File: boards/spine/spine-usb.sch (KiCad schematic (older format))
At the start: 36 parts, among them P1 USB_B, U1 93C56, U2 FT2232H, Y1 12 MHz

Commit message: Power management and such
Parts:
- P1: value USB_B -> USB-B
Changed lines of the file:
@@
 P 1150 2550
 F 0 "P1" V 850 2650 50  0000 C CNN
-F 1 "USB_B" H 1100 2750 50  0000 C CNN
+F 1 "USB-B" H 1100 2750 50  0000 C CNN
 F 2 "" V 1100 2450 60  0000 C CNN
 F 3 "http://productfinder.pulseeng.com/products/datasheets/E8144-B02022-L.PDF" V 1100 2450 60  0001 C CNN
@@
 $EndComp
 $Comp
-L GND #PWR1
+L GND #PWR01
 U 1 1 563F3C00
 P 1050 4000
-F 0 "#PWR1" H 1050 3750 50  0001 C CNN
+F 0 "#PWR01" H 1050 3750 50  0001 C CNN
 F 1 "GND" H 1050 3850 50  0000 C CNN
 F 2 "" H 1050 4000 60  0000 C CNN
@@
 $EndComp
 $Comp
-L +3V3 #PWR11
+L +3V3 #PWR02
 U 1 1 563F5B33
 P 4500 1350
-F 0 "#PWR11" H 4500 1200 50  0001 C CNN
+F 0 "#PWR02" H 4500 1200 50  0001 C CNN
 F 1 "+3V3" H 4500 1490 50  0000 C CNN
 F 2 "" H 4500 1350 60  0000 C CNN
@@
 NoConn ~ 1950 3800
 $Comp
-L GND #PWR12
+L GND #PWR03
 U 1 1 56407FC9
 P 4500 3550
-F 0 "#PWR12" H 4500 3300 50  0001 C CNN
+F 0 "#PWR03" H 4500 3300 50  0001 C CNN
 F 1 "GND" H 4500 3400 50  0000 C CNN
 F 2 "" H 4500 3550 60  0000 C CNN
@@
 $EndComp
 $Comp
-L +3V3 #PWR16
+L +3V3 #PWR04
 U 1 1 56409B2C
 P 7350 950
-F 0 "#PWR16" H 7350 800 50  0001 C CNN
+F 0 "#PWR04" H 7350 800 50  0001 C CNN
 F 1 "+3V3" H 7350 1090 50  0000 C CNN
 F 2 "" H 7350 950 60  0000 C CNN
@@
 $EndComp
 $Comp
-L +3V3 #PWR2
+L +3V3 #PWR05
 U 1 1 5640C498
 P 1050 5000
-F 0 "#PWR2" H 1050 4850 50  0001 C CNN
+F 0 "#PWR05" H 1050 4850 50  0001 C CNN
 F 1 "+3V3" H 1050 5140 50  0000 C CNN
 F 2 "" H 1050 5000 60  0000 C CNN
@@
 $EndComp
 $Comp
-L GND #PWR3
+L GND #PWR06
 U 1 1 5640C700
 P 1050 5800
-F 0 "#PWR3" H 1050 5550 50  0001 C CNN
+F 0 "#PWR06" H 1050 5550 50  0001 C CNN
 F 1 "GND" H 1050 5650 50  0000 C CNN
 F 2 "" H 1050 5800 60  0000 C CNN
@@
 $EndComp
 $Comp
-L +3V3 #PWR5
+L +3V3 #PWR07
 U 1 1 5640CB0D
 P 2800 4500
-F 0 "#PWR5" H 2800 4350 50  0001 C CNN
+F 0 "#PWR07" H 2800 4350 50  0001 C CNN
 F 1 "+3V3" H 2800 4640 50  0000 C CNN
 F 2 "" H 2800 4500 60  0000 C CNN
@@
 $EndComp
 $Comp
-L GND #PWR4
+L GND #PWR08
 U 1 1 5640EC58
 P 1750 7450
-F 0 "#PWR4" H 1750 7200 50  0001 C CNN
+F 0 "#PWR08" H 1750 7200 50  0001 C CNN
 F 1 "GND" H 1750 7300 50  0000 C CNN
 F 2 "" H 1750 7450 60  0000 C CNN
@@
 $EndComp
 $Comp
-L GND #PWR7
+L GND #PWR09
 U 1 1 5640ECEA
 P 2900 1650
-F 0 "#PWR7" H 2900 1400 50  0001 C CNN
+F 0 "#PWR09" H 2900 1400 50  0001 C CNN
 F 1 "GND" H 2900 1500 50  0000 C CNN
 F 2 "" H 2900 1650 60  0000 C CNN
@@
 FTDI_1V8REG
 $Comp
-L +3V3 #PWR6
+L +3V3 #PWR010
 U 1 1 5640F443
 P 2900 1000
-F 0 "#PWR6" H 2900 850 50  0001 C CNN
+F 0 "#PWR010" H 2900 850 50  0001 C CNN
 F 1 "+3V3" H 2900 1140 50  0000 C CNN
 F 2 "" H 2900 1000 60  0000 C CNN
@@
 $EndComp
 $Comp
-L GND #PWR10
+L GND #PWR011
 U 1 1 56411C34
 P 4450 5800
-F 0 "#PWR10" H 4450 5550 50  0001 C CNN
+F 0 "#PWR011" H 4450 5550 50  0001 C CNN
 F 1 "GND" H 4450 5650 50  0000 C CNN
 F 2 "" H 4450 5800 60  0000 C CNN
@@
 $EndComp
 $Comp
-L GND #PWR15
+L GND #PWR012
 U 1 1 56412014
 P 6450 5800
-F 0 "#PWR15" H 6450 5550 50  0001 C CNN
+F 0 "#PWR012" H 6450 5550 50  0001 C CNN
 F 1 "GND" H 6450 5650 50  0000 C CNN
 F 2 "" H 6450 5800 60  0000 C CNN
@@
 $EndComp
 $Comp
-L GND #PWR9
+L GND #PWR013
 U 1 1 5642A93B
 P 3400 7450
-F 0 "#PWR9" H 3400 7200 50  0001 C CNN
+F 0 "#PWR013" H 3400 7200 50  0001 C CNN
 F 1 "GND" H 3400 7300 50  0000 C CNN
 F 2 "" H 3400 7450 60  0000 C CNN
@@
 	3700 7400 3700 7300
 $Comp
-L +3V3 #PWR8
+L +3V3 #PWR014
 U 1 1 5642B955
 P 3400 6450
-F 0 "#PWR8" H 3400 6300 50  0001 C CNN
+F 0 "#PWR014" H 3400 6300 50  0001 C CNN
 F 1 "+3V3" H 3400 6590 50  0000 C CNN
 F 2 "" H 3400 6450 60  0000 C CNN
@@
 $EndComp
 $Comp
-L GND #PWR14
+L GND #PWR015
 U 1 1 5642BC5C
 P 4750 7450
-F 0 "#PWR14" H 4750 7200 50  0001 C CNN
+F 0 "#PWR015" H 4750 7200 50  0001 C CNN
 F 1 "GND" H 4750 7300 50  0000 C CNN
 F 2 "" H 4750 7450 60  0000 C CNN
@@
 	5050 7400 5050 7300
 $Comp
-L +3V3 #PWR13
+L +3V3 #PWR016
 U 1 1 5642BC76
 P 4750 6450
-F 0 "#PWR13" H 4750 6300 50  0001 C CNN
+F 0 "#PWR016" H 4750 6300 50  0001 C CNN
 F 1 "+3V3" H 4750 6590 50  0000 C CNN
 F 2 "" H 4750 6450 60  0000 C CNN

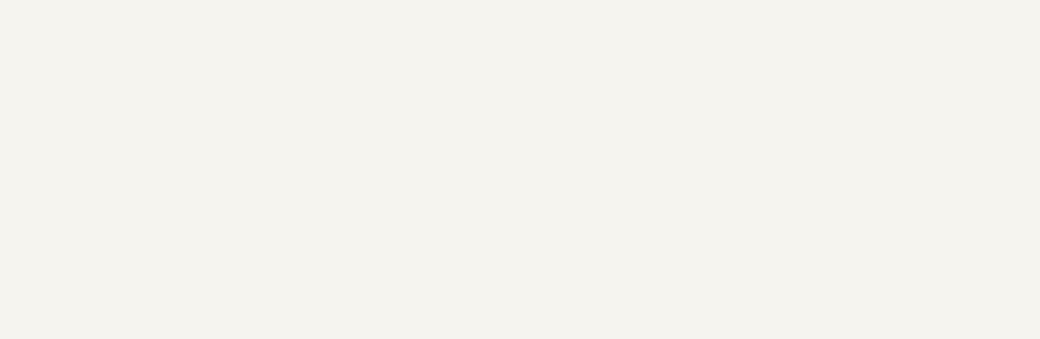
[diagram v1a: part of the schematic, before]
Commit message: Clock generator, sync connectors, title blocks
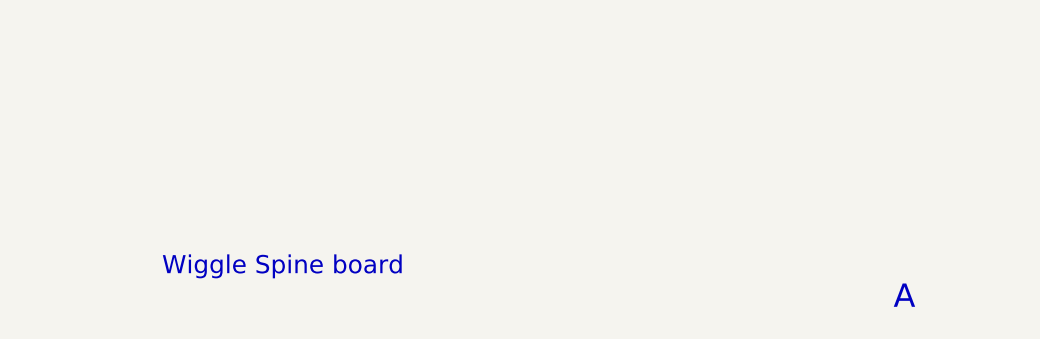
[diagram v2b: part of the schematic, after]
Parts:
- C1, C11, C12, C14, C16, C2, C3, C4, C5, C6, C7, C8, C9: footprint 0805 -> Capacitors_SMD:C_0805
- C10, C13, C15, C17: footprint 1206 -> Capacitors_SMD:C_1206
- R1, R10, R2, R3, R4, R5, R6, R7, R8, R9: footprint (none) -> Resistors_SMD:R_0805
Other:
- note added: "A"
- note added: "Wiggle Spine board"

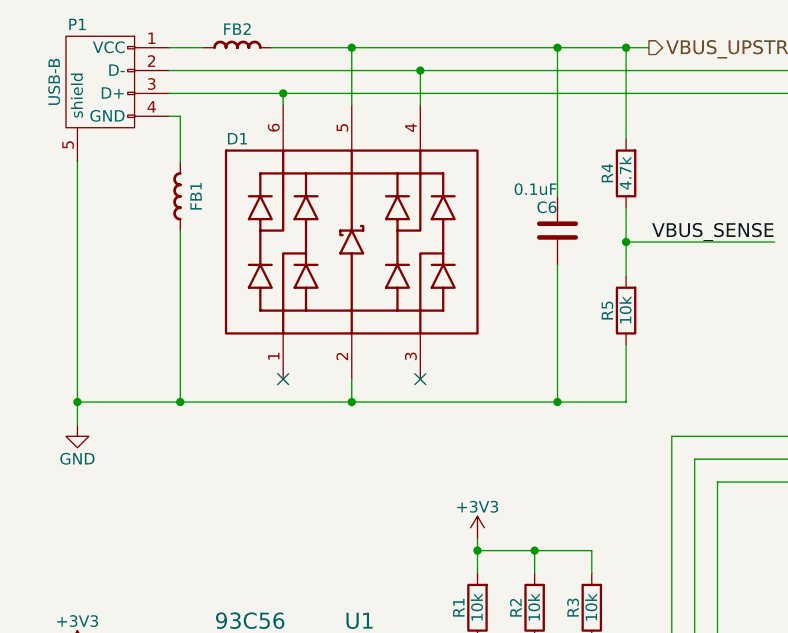
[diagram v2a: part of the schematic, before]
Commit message: Fixes for shield grounds and module numbering
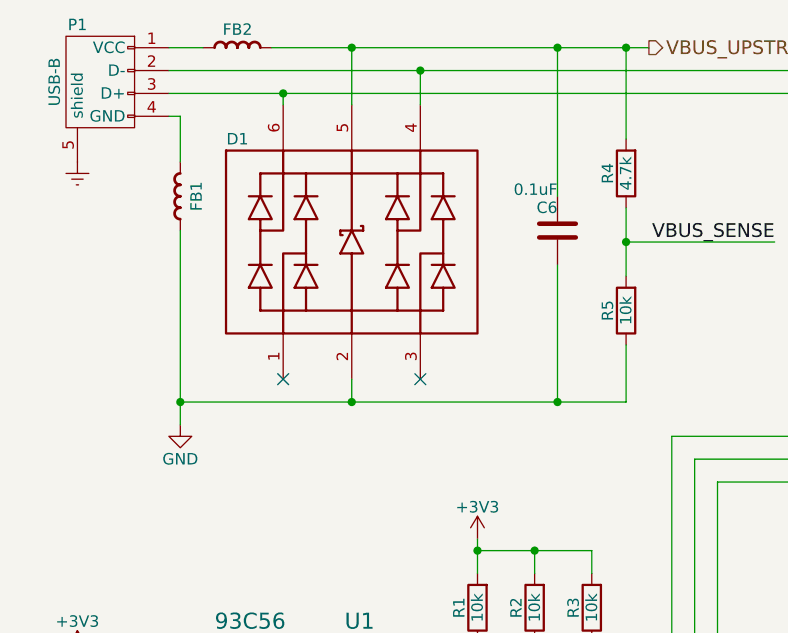
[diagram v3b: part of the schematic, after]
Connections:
- net labels added: Earth
- wire segments 146 -> 145
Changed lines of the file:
@@
 L GND #PWR01
 U 1 1 563F3C00
-P 1050 4000
-F 0 "#PWR01" H 1050 3750 50  0001 C CNN
-F 1 "GND" H 1050 3850 50  0000 C CNN
-F 2 "" H 1050 4000 60  0000 C CNN
-F 3 "" H 1050 4000 60  0000 C CNN
-	1    1050 4000
+P 1500 4000
+F 0 "#PWR01" H 1500 3750 50  0001 C CNN
+F 1 "GND" H 1500 3850 50  0000 C CNN
+F 2 "" H 1500 4000 60  0000 C CNN
+F 3 "" H 1500 4000 60  0000 C CNN
+	1    1500 4000
 	1    0    0    -1
 $EndComp
@@
 Connection ~ 2250 2350
 Wire Wire Line
-	1050 2850 1050 4000
-Wire Wire Line
-	1050 3900 3450 3900
-Wire Wire Line
 	2250 3900 2250 3800
 Wire Wire Line
 	1500 2650 1500 2850
-Connection ~ 1050 3900
 Wire Wire Line
-	1500 3150 1500 3900
+	1500 3150 1500 4000
 Connection ~ 1500 3900
 Wire Wire Line
@@
 FB 59 00 E6 A5 69 3A 37 9E CF 73 BC F7 37 E3 33 5D 9E A8 3E 7F 80 FA F7 F6 BB 44 F4 6E D4 E7 77
 A2 1E 1F 27 A2 E3 16 70 32 E9 54 FE 3F E7 AF 00 CA 1C A3 36 0A 00 00 00 00 49 45 4E 44 AE 42 60
-82 EC
+82 00
 EndData
 $EndBitmap
@@
 72 0F 1C A9 DC 70 49 CB 79 33 88 85 99 AD 01 6C 4B 10 FC 3B 13 DE 3B 37 68 79 AD 07 BC 00 3C 0E
 3C 31 EE E3 D8 E7 0F 03 D7 7B 9F FB C1 E1 FF 01 18 C4 96 1D B8 0E 40 07 00 00 00 00 49 45 4E 44
-AE 42 60 82 FF
+AE 42 60 82 00
 EndData
 $EndBitmap
 Text Notes 9900 7900 0    102  ~ 0
 A
+Wire Wire Line
+	1500 3900 3450 3900
+$Comp
+L Earth #PWR017
+U 1 1 565B7DB6
+P 1050 2850
+F 0 "#PWR017" H 1050 2600 50  0001 C CNN
+F 1 "Earth" H 1050 2700 50  0001 C CNN
+F 2 "" H 1050 2850 60  0000 C CNN
+F 3 "" H 1050 2850 60  0000 C CNN
+	1    1050 2850
+	1    0    0    -1
+$EndComp
 $EndSCHEMATC

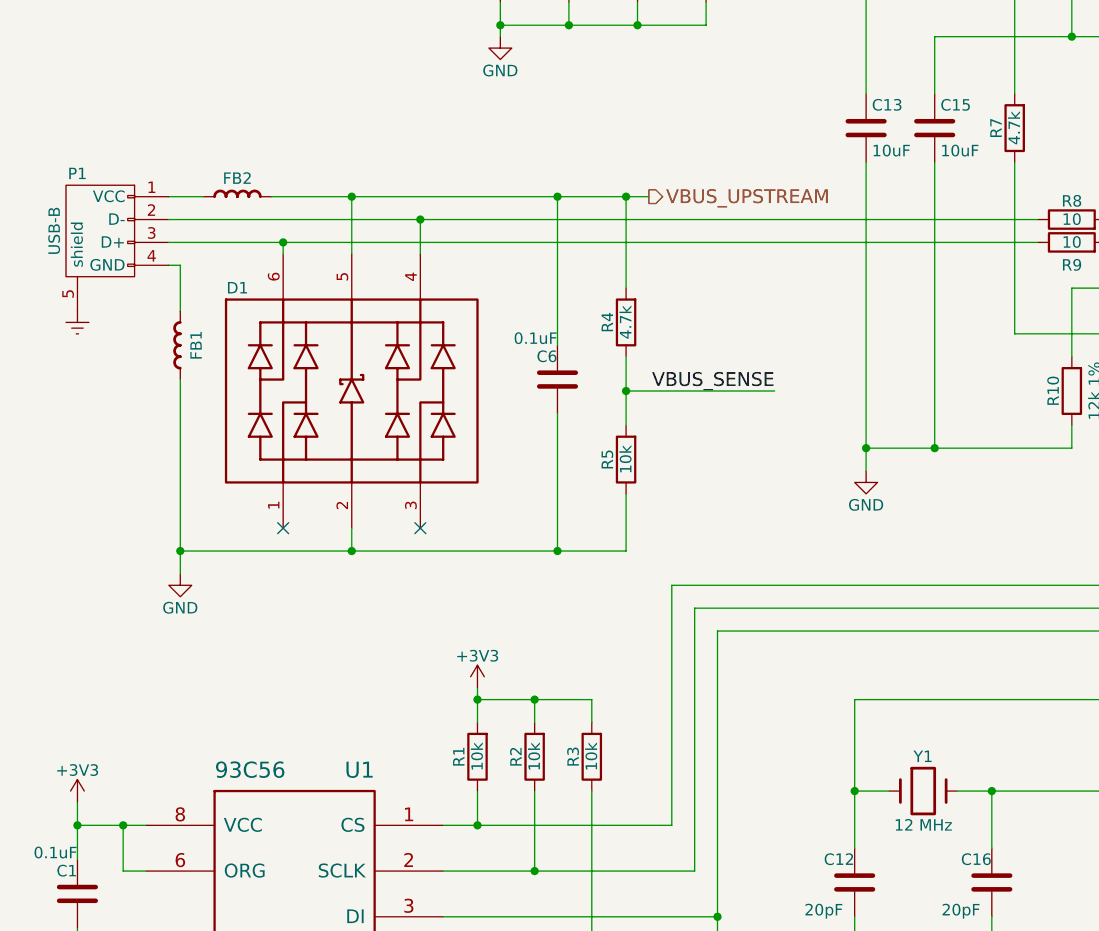
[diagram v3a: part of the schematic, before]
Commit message: Schematic footprint and refdes work
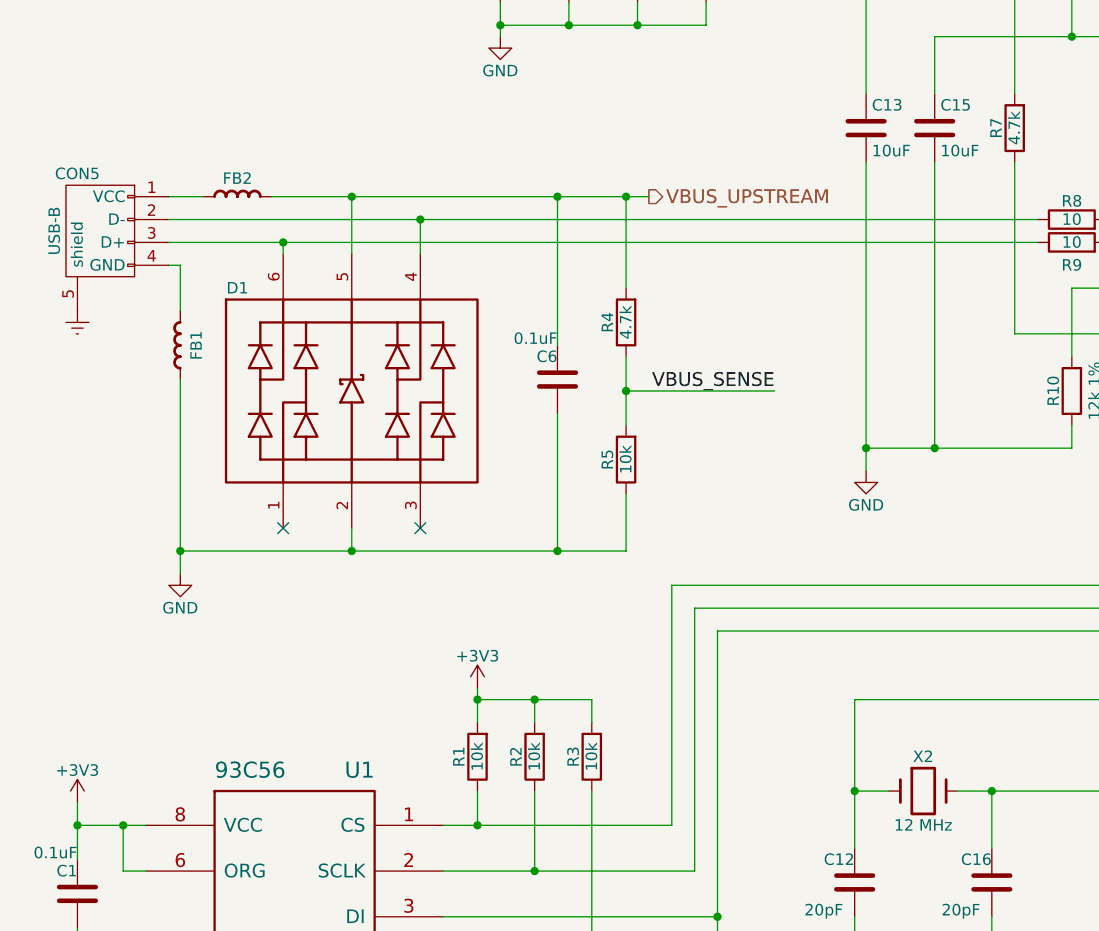
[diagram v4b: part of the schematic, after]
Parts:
- C1: footprint Capacitors_SMD:C_0805 -> TO_SOT_Packages_SMD:SOT-886
- CON5: renamed from P1; footprint (none) -> Connect:USB_B
- D1: footprint (none) -> SOT363:SOT363
- FB1, FB2, FB3, FB4: footprint (none) -> Resistors_SMD:R_0805
- U1: footprint (none) -> Housings_SOIC:SOIC-8_3.9x4.9mm_Pitch1.27mm
- U2: footprint (none) -> Housings_QFP:LQFP-64_10x10mm_Pitch0.5mm
- X2: renamed from Y1; footprint (none) -> Crystals:Crystal_HC49-SD_SMD
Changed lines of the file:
@@
 $EndDescr
 $Comp
-L USB_B P1
+L USB_B CON5
 U 1 1 5637E4EA
 P 1150 2550
-F 0 "P1" V 850 2650 50  0000 C CNN
+F 0 "CON5" V 850 2650 50  0000 C CNN
 F 1 "USB-B" H 1100 2750 50  0000 C CNN
-F 2 "" V 1100 2450 60  0001 C CNN
+F 2 "Connect:USB_B" V 1100 2450 60  0001 C CNN
 F 3 "http://productfinder.pulseeng.com/products/datasheets/E8144-B02022-L.PDF" V 1100 2450 60  0001 C CNN
 F 4 "Digikey" H 1150 2550 60  0001 C CNN "Vend1"
@@
 F 0 "FB2" H 1750 2400 50  0000 C BNN
 F 1 "Ferrite bead" H 2000 2400 39  0001 C BNN
-F 2 "" H 1600 2500 50  0001 C CNN
+F 2 "Resistors_SMD:R_0805" H 1600 2500 50  0001 C CNN
 F 3 "http://www.samsungsem.com/kr/front/downloadcms.do?path=/kr/support/product-search/bead/__icsFiles/afieldfile/2014/11/13&fileName=S_CIB21P110NE.pdf" H 1625 2350 60  0001 C CNN
 F 4 "0.00906" H 1600 2350 60  0001 C CNN "RefPrice1k"
@@
 F 0 "FB1" H 1650 3050 50  0000 C BNN
 F 1 "Ferrite bead" H 1900 3050 39  0001 C BNN
-F 2 "" H 1500 3300 50  0001 C CNN
+F 2 "Resistors_SMD:R_0805" H 1500 3300 50  0001 C CNN
 F 3 "http://www.samsungsem.com/kr/front/downloadcms.do?path=/kr/support/product-search/bead/__icsFiles/afieldfile/2014/11/13&fileName=S_CIB21P110NE.pdf" H 1525 3150 60  0001 C CNN
 F 4 "0.00906" H 1500 3150 60  0001 C CNN "RefPrice1k"
@@
 F 0 "U2" H 5800 5450 50  0000 L CNN
 F 1 "FT2232H" H 7600 5450 50  0000 L CNN
-F 2 "" H 6850 3350 50  0001 C CNN
+F 2 "Housings_QFP:LQFP-64_10x10mm_Pitch0.5mm" H 6850 3350 50  0001 C CNN
 F 3 "http://www.ftdichip.com/Support/Documents/DataSheets/ICs/DS_FT2232H.pdf" H 6850 3350 50  0001 C CNN
 F 4 "3.70" H 6850 3350 60  0001 C CNN "RefPrice1k"
@@
 $EndComp
 $Comp
-L GND #PWR01
+L GND #PWR4
 U 1 1 563F3C00
 P 1500 4000
-F 0 "#PWR01" H 1500 3750 50  0001 C CNN
+F 0 "#PWR4" H 1500 3750 50  0001 C CNN
 F 1 "GND" H 1500 3850 50  0000 C CNN
 F 2 "" H 1500 4000 60  0000 C CNN
@@
 $EndComp
 $Comp
-L +3V3 #PWR02
+L +3V3 #PWR12
 U 1 1 563F5B33
 P 4500 1350
-F 0 "#PWR02" H 4500 1200 50  0001 C CNN
+F 0 "#PWR12" H 4500 1200 50  0001 C CNN
 F 1 "+3V3" H 4500 1490 50  0000 C CNN
 F 2 "" H 4500 1350 60  0000 C CNN
@@
 F 0 "D1" H 1750 3550 50  0000 C CNN
 F 1 "TVS DIODE 5.5VWM" H 2250 2350 50  0001 C CNN
-F 2 "" V 2700 3050 60  0001 C CNN
+F 2 "SOT363:SOT363" V 2700 3050 60  0001 C CNN
 F 3 "http://www.nxp.com/documents/data_sheet/PRTR5V0U4Y.pdf" V 2700 3050 60  0001 C CNN
 F 4 "NXP" H 2250 3150 60  0001 C CNN "MfrId"
@@
 NoConn ~ 1950 3800
 $Comp
-L GND #PWR03
+L GND #PWR13
 U 1 1 56407FC9
 P 4500 3550
-F 0 "#PWR03" H 4500 3300 50  0001 C CNN
+F 0 "#PWR13" H 4500 3300 50  0001 C CNN
 F 1 "GND" H 4500 3400 50  0000 C CNN
 F 2 "" H 4500 3550 60  0000 C CNN
@@
 F 0 "FB3" H 3550 6500 50  0000 C BNN
 F 1 "Ferrite bead" H 3800 6500 39  0001 C BNN
-F 2 "" H 3400 6600 50  0001 C CNN
+F 2 "Resistors_SMD:R_0805" H 3400 6600 50  0001 C CNN
 F 3 "http://www.samsungsem.com/kr/front/downloadcms.do?path=/kr/support/product-search/bead/__icsFiles/afieldfile/2014/11/13&fileName=S_CIB21P110NE.pdf" H 3425 6450 60  0001 C CNN
 F 4 "0.00906" H 3400 6450 60  0001 C CNN "RefPrice1k"
@@
 $EndComp
 $Comp
-L +3V3 #PWR04
+L +3V3 #PWR17
 U 1 1 56409B2C
 P 7350 950
-F 0 "#PWR04" H 7350 800 50  0001 C CNN
+F 0 "#PWR17" H 7350 800 50  0001 C CNN
 F 1 "+3V3" H 7350 1090 50  0000 C CNN
 F 2 "" H 7350 950 60  0000 C CNN
@@
 F 0 "U1" H 2350 6100 70  0000 R BNN
 F 1 "93C56" H 1650 6100 70  0000 L BNN
-F 2 "" H 2000 5500 60  0001 C CNN
+F 2 "Housings_SOIC:SOIC-8_3.9x4.9mm_Pitch1.27mm" H 2000 5500 60  0001 C CNN
 F 3 "http://www.onsemi.com/pub_link/Collateral/CAT93C56-D.PDF" H 2000 5500 60  0001 C CNN
 F 4 "Digikey" H 2000 5500 60  0001 C CNN "Vend1"
@@
 $EndComp
 $Comp
-L +3V3 #PWR05
+L +3V3 #PWR2
 U 1 1 5640C498
 P 1050 5000
-F 0 "#PWR05" H 1050 4850 50  0001 C CNN
+F 0 "#PWR2" H 1050 4850 50  0001 C CNN
 F 1 "+3V3" H 1050 5140 50  0000 C CNN
 F 2 "" H 1050 5000 60  0000 C CNN
@@
 $EndComp
 $Comp
-L GND #PWR06
+L GND #PWR3
 U 1 1 5640C700
 P 1050 5800
-F 0 "#PWR06" H 1050 5550 50  0001 C CNN
+F 0 "#PWR3" H 1050 5550 50  0001 C CNN
 F 1 "GND" H 1050 5650 50  0000 C CNN
 F 2 "" H 1050 5800 60  0000 C CNN
@@
 $EndComp
 $Comp
-L +3V3 #PWR07
+L +3V3 #PWR6
 U 1 1 5640CB0D
 P 2800 4500
-F 0 "#PWR07" H 2800 4350 50  0001 C CNN
+F 0 "#PWR6" H 2800 4350 50  0001 C CNN
 F 1 "+3V3" H 2800 4640 50  0000 C CNN
 F 2 "" H 2800 4500 60  0000 C CNN
@@
 $EndComp
 $Comp
-L GND #PWR08
+L GND #PWR5
 U 1 1 5640EC58
 P 1750 7450
-F 0 "#PWR08" H 1750 7200 50  0001 C CNN
+F 0 "#PWR5" H 1750 7200 50  0001 C CNN
 F 1 "GND" H 1750 7300 50  0000 C CNN
 F 2 "" H 1750 7450 60  0000 C CNN
@@
 $EndComp
 $Comp
-L GND #PWR09
+L GND #PWR8
 U 1 1 5640ECEA
 P 2900 1650
-F 0 "#PWR09" H 2900 1400 50  0001 C CNN
+F 0 "#PWR8" H 2900 1400 50  0001 C CNN
 F 1 "GND" H 2900 1500 50  0000 C CNN
 F 2 "" H 2900 1650 60  0000 C CNN
@@
 FTDI_1V8REG
 $Comp
-L +3V3 #PWR010
+L +3V3 #PWR7
 U 1 1 5640F443
 P 2900 1000
-F 0 "#PWR010" H 2900 850 50  0001 C CNN
+F 0 "#PWR7" H 2900 850 50  0001 C CNN
 F 1 "+3V3" H 2900 1140 50  0000 C CNN
 F 2 "" H 2900 1000 60  0000 C CNN
@@
 NoConn ~ 8050 5150
 $Comp
-L Crystal Y1
+L Crystal X2
 U 1 1 564105F5
 P 4750 4950
-F 0 "Y1" H 4750 5100 50  0000 C CNN
+F 0 "X2" H 4750 5100 50  0000 C CNN
 F 1 "12 MHz" H 4750 4800 50  0000 C CNN
-F 2 "" H 4750 4950 60  0001 C CNN
+F 2 "Crystals:Crystal_HC49-SD_SMD" H 4750 4950 60  0001 C CNN
 F 3 "http://www.abracon.com/Resonators/abls.pdf" H 4750 4950 60  0001 C CNN
 F 4 "0.172" H 4750 4950 60  0001 C CNN "RefPrice1k"
@@
 $EndComp
 $Comp
-L GND #PWR011
+L GND #PWR11
 U 1 1 56411C34
 P 4450 5800
-F 0 "#PWR011" H 4450 5550 50  0001 C CNN
+F 0 "#PWR11" H 4450 5550 50  0001 C CNN
 F 1 "GND" H 4450 5650 50  0000 C CNN
 F 2 "" H 4450 5800 60  0000 C CNN
@@
 $EndComp
 $Comp
-L GND #PWR012
+L GND #PWR16
 U 1 1 56412014
 P 6450 5800
-F 0 "#PWR012" H 6450 5550 50  0001 C CNN
+F 0 "#PWR16" H 6450 5550 50  0001 C CNN
 F 1 "GND" H 6450 5650 50  0000 C CNN
 F 2 "" H 6450 5800 60  0000 C CNN
@@
 F 0 "C1" H 1050 5300 50  0000 L CNN
 F 1 "0.1uF" H 1050 5250 50  0000 L TNN
-F 2 "Capacitors_SMD:C_0805" H 1088 5250 30  0001 C CNN
+F 2 "TO_SOT_Packages_SMD:SOT-886" H 1088 5250 30  0001 C CNN
 F 3 "http://psearch.murata.com/capacitor/product/GRM21BR71H104MA01%23.pdf" H 1050 5400 60  0001 C CNN
 F 4 "0.01880" V 1050 5400 60  0001 C CNN "RefPrice1k"
@@
 $EndComp
 $Comp
-L GND #PWR013
+L GND #PWR10
 U 1 1 5642A93B
 P 3400 7450
-F 0 "#PWR013" H 3400 7200 50  0001 C CNN
+F 0 "#PWR10" H 3400 7200 50  0001 C CNN
 F 1 "GND" H 3400 7300 50  0000 C CNN
 F 2 "" H 3400 7450 60  0000 C CNN
@@
 	3700 7400 3700 7300
 $Comp
-L +3V3 #PWR014
+L +3V3 #PWR9
 U 1 1 5642B955
 P 3400 6450
-F 0 "#PWR014" H 3400 6300 50  0001 C CNN
+F 0 "#PWR9" H 3400 6300 50  0001 C CNN
 F 1 "+3V3" H 3400 6590 50  0000 C CNN
 F 2 "" H 3400 6450 60  0000 C CNN
@@
 F 0 "FB4" H 4900 6500 50  0000 C BNN
 F 1 "Ferrite bead" H 5150 6500 39  0001 C BNN
-F 2 "" H 4750 6600 50  0001 C CNN
+F 2 "Resistors_SMD:R_0805" H 4750 6600 50  0001 C CNN
 F 3 "http://www.samsungsem.com/kr/front/downloadcms.do?path=/kr/support/product-search/bead/__icsFiles/afieldfile/2014/11/13&fileName=S_CIB21P110NE.pdf" H 4775 6450 60  0001 C CNN
 F 4 "0.00906" H 4750 6450 60  0001 C CNN "RefPrice1k"
@@
 $EndComp
 $Comp
-L GND #PWR015
+L GND #PWR15
 U 1 1 5642BC5C
 P 4750 7450
-F 0 "#PWR015" H 4750 7200 50  0001 C CNN
+F 0 "#PWR15" H 4750 7200 50  0001 C CNN
 F 1 "GND" H 4750 7300 50  0000 C CNN
 F 2 "" H 4750 7450 60  0000 C CNN
@@
 	5050 7400 5050 7300
 $Comp
-L +3V3 #PWR016
+L +3V3 #PWR14
 U 1 1 5642BC76
 P 4750 6450
-F 0 "#PWR016" H 4750 6300 50  0001 C CNN
+F 0 "#PWR14" H 4750 6300 50  0001 C CNN
 F 1 "+3V3" H 4750 6590 50  0000 C CNN
 F 2 "" H 4750 6450 60  0000 C CNN
@@
 	1500 3900 3450 3900
 $Comp
-L Earth #PWR017
+L Earth #PWR1
 U 1 1 565B7DB6
 P 1050 2850
-F 0 "#PWR017" H 1050 2600 50  0001 C CNN
+F 0 "#PWR1" H 1050 2600 50  0001 C CNN
 F 1 "Earth" H 1050 2700 50  0001 C CNN
 F 2 "" H 1050 2850 60  0000 C CNN
